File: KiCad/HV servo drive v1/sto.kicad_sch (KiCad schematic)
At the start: 41 parts, among them J9 Conn_02x03_Top_Bottom, Q8 PMOS, U16 6N137, U17 6N137, U18 FODM217A, U19 FODM217A

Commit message: KiCad 8.0 update
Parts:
- renumbered C97 to C96, C98 to C97, C96 to C98, D27 to D11, D26 to D25, D25 to D26, D28 to D27, D30 to D28, D29 to D7, J9 to J1, Q8 to Q7, R69 to R15, R73 to R16, R72 to R17, R77 to R31, R78 to R32, R83 to R65, R84 to R67, R79 to R69, R70 to R7, R71 to R70, R86 to R71, R85 to R72, R76 to R73, R80 to R74, R81 to R76, R74 to R77, R82 to R78, R67 to R8, R65 to R9, TP22 to TP18, TP23 to TP19, TP24 to TP20

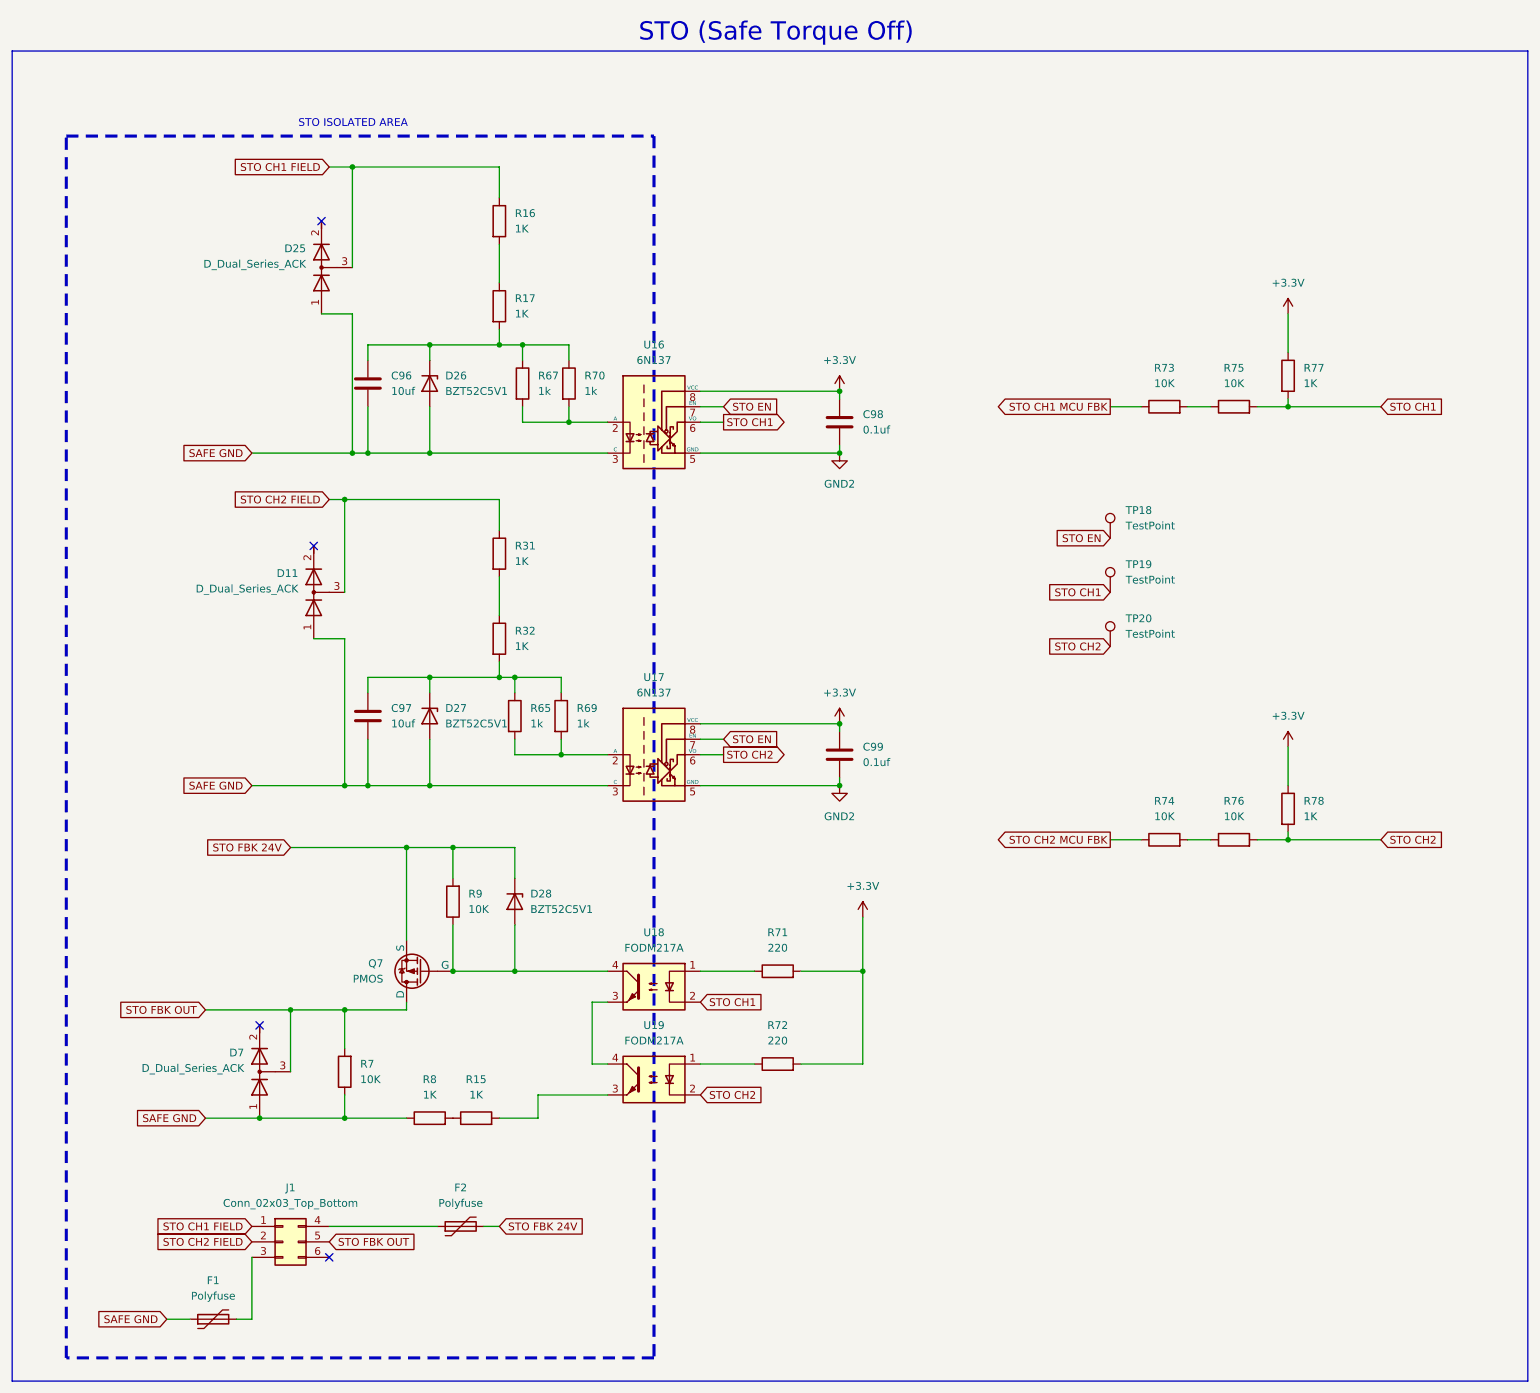
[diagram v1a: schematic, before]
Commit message: start rev 2 changes
fix component references, fix rj45 and dc-dc converter footprints, add RLC filters on all power connectors, add more mounting holes
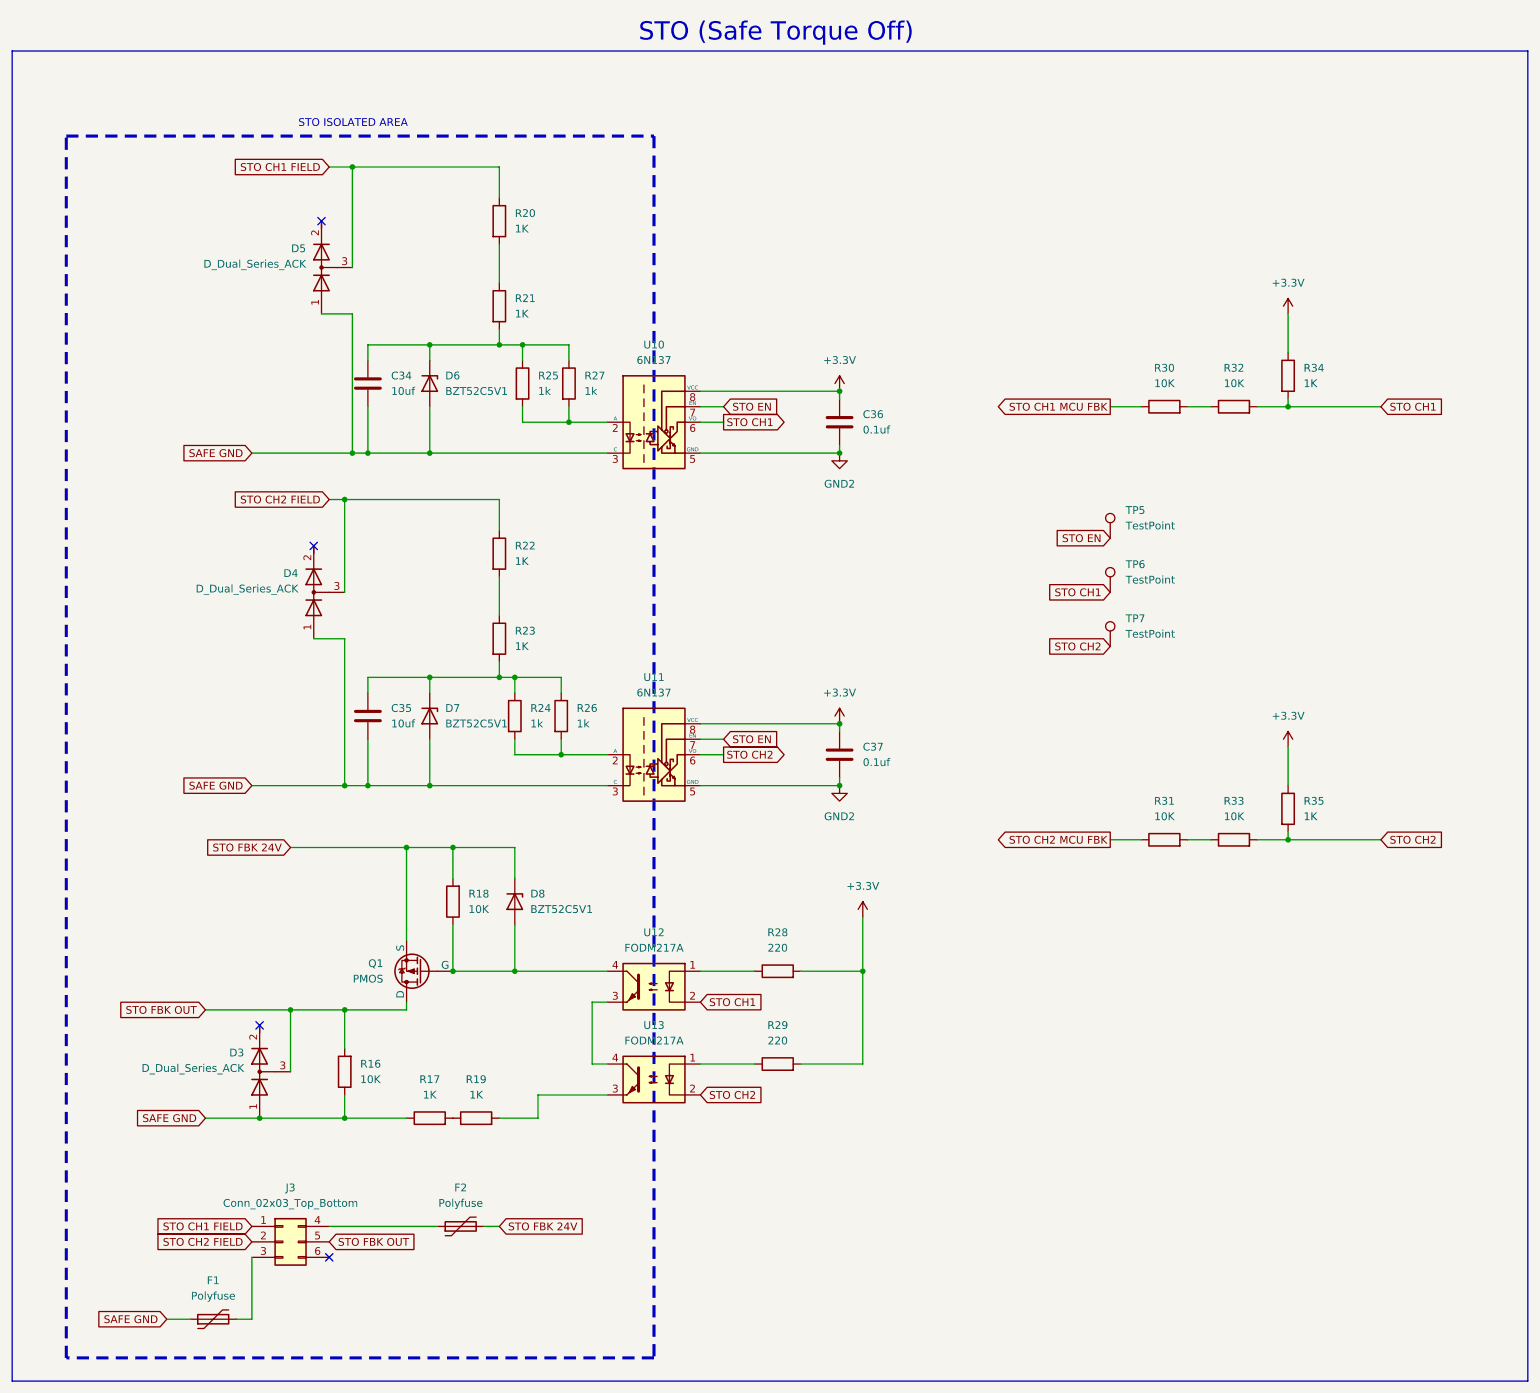
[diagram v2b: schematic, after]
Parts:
- renumbered C96 to C34, C97 to C35, C98 to C36, C99 to C37, D7 to D3, D11 to D4, D25 to D5, D26 to D6, D27 to D7, D28 to D8, J1 to J3, Q7 to Q1, R7 to R16, R8 to R17, R9 to R18, R15 to R19, R16 to R20, R17 to R21, R31 to R22, R32 to R23, R65 to R24, R67 to R25, R69 to R26, R70 to R27, R71 to R28, R72 to R29, R73 to R30, R74 to R31, R75 to R32, R76 to R33, R77 to R34, R78 to R35, TP18 to TP5, TP19 to TP6, TP20 to TP7, U16 to U10, U17 to U11, U18 to U12, U19 to U13

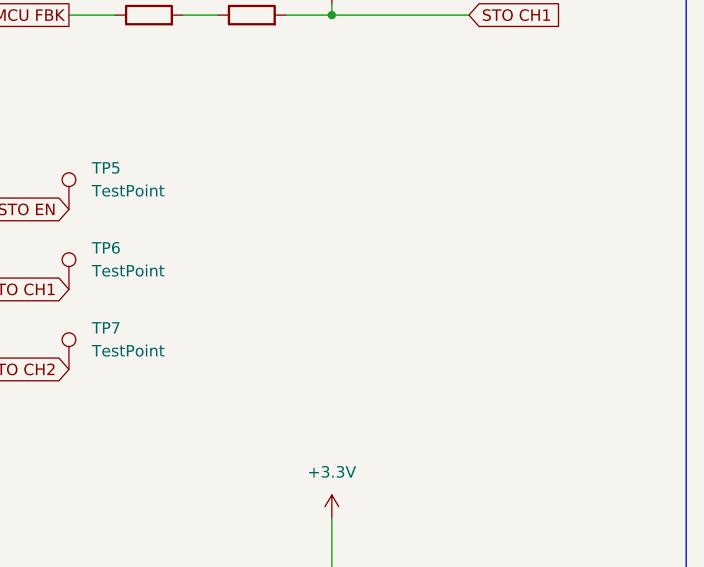
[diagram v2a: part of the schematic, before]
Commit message: add STO enable pulldown for MCU
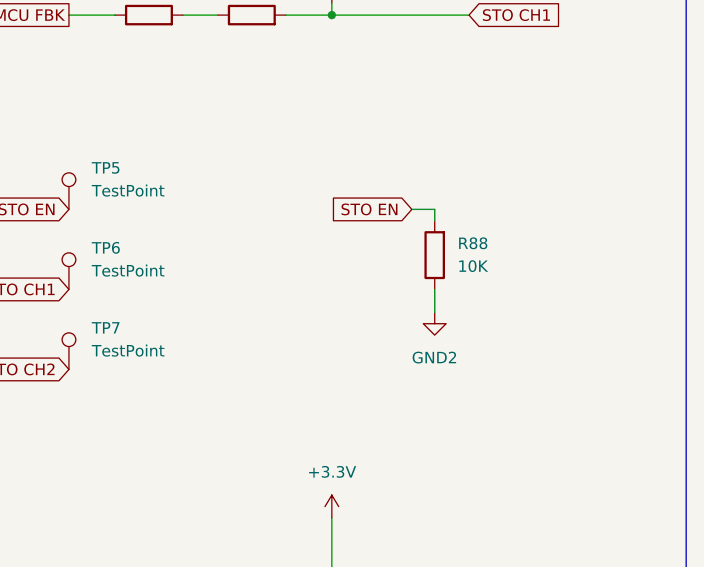
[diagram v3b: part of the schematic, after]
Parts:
- added R88: 10K, Resistor_SMD:R_0603_1608Metric, symbol Device:R
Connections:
- net GND2: now also R88.1
- net STO EN: now also R88.2
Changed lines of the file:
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@@
 	(wire
 		(pts
+			(xy 254 114.3) (xy 254 113.03)
+		)
+		(stroke
+			(width 0)
+			(type default)
+		)
+	)
+	(wire
+		(pts
 			(xy 226.06 91.44) (xy 229.87 91.44)
 		)
@@
 	(wire
 		(pts
+			(xy 251.46 113.03) (xy 254 113.03)
+		)
+		(stroke
+			(width 0)
+			(type default)
+		)
+	)
+	(wire
+		(pts
 			(xy 105.41 176.53) (xy 105.41 184.15)
 		)
@@
 	(wire
 		(pts
+			(xy 254 121.92) (xy 254 124.46)
+		)
+		(stroke
+			(width 0)
+			(type default)
+		)
+	)
+	(wire
+		(pts
 			(xy 124.46 81.28) (xy 116.84 81.28)
 		)
@@
 		)
 	)
+	(global_label "STO EN"
+		(shape input)
+		(at 251.46 113.03 180)
+		(fields_autoplaced yes)
+		(effects
+			(font
+				(size 1.27 1.27)
+			)
+			(justify right)
+		)
+		(property "Intersheetrefs" "${INTERSHEET_REFS}"
+			(at 241.5201 113.03 0)
+			(effects
+				(font
+					(size 1.27 1.27)
+				)
+				(justify right)
+				(hide yes)
+			)
+		)
+	)
 	(global_label "STO CH1"
 		(shape input)
@@
 	)
 	(symbol
+		(lib_id "Device:R")
+		(at 254 118.11 180)
+		(unit 1)
+		(exclude_from_sim no)
+		(in_bom yes)
+		(on_board yes)
+		(dnp no)
+		(fields_autoplaced yes)
+		(property "Reference" "R88"
+			(at 256.54 116.8399 0)
+			(effects
+				(font
+					(size 1.27 1.27)
+				)
+				(justify right)
+			)
+		)
+		(property "Value" "10K"
+			(at 256.54 119.3799 0)
+			(effects
+				(font
+					(size 1.27 1.27)
+				)
+				(justify right)
+			)
+		)
+		(property "Footprint" "Resistor_SMD:R_0603_1608Metric"
+			(at 255.778 118.11 90)
+			(effects
+				(font
+					(size 1.27 1.27)
+				)
+				(hide yes)
+			)
+		)
+		(property "Datasheet" "~"
+			(at 254 118.11 0)
+			(effects
+				(font
+					(size 1.27 1.27)
+				)
+				(hide yes)
+			)
+		)
+		(property "Description" ""
+			(at 254 118.11 0)
+			(effects
+				(font
+					(size 1.27 1.27)
+				)
+				(hide yes)
+			)
+		)
+		(pin "1"
+		)
+		(pin "2"
+		)
+		(instances
+			(project "HV servo drive v1"
+				(path "/00e1489f-e855-42b2-9b8a-dcc958a4feb6/5ac84363-ab69-4569-a1a9-ce084738114b"
+					(reference "R88")
+					(unit 1)
+				)
+			)
+		)
+	)
+	(symbol
 		(lib_id "Connector_Generic:Conn_02x03_Top_Bottom")
 		(at 77.47 228.6 0)
@@
 					(unit 1)
 				)
+			)
+		)
+	)
+	(symbol
+		(lib_id "power:GND2")
+		(at 254 124.46 0)
+		(unit 1)
+		(exclude_from_sim no)
+		(in_bom yes)
+		(on_board yes)
+		(dnp no)
+		(fields_autoplaced yes)
+		(property "Reference" "#PWR0141"
+			(at 254 130.81 0)
+			(effects
+				(font
+					(size 1.27 1.27)
+				)
+				(hide yes)
+			)
+		)
+		(property "Value" "GND2"
+			(at 254 129.54 0)
+			(effects
+				(font
+					(size 1.27 1.27)
+				)
+			)
+		)
+		(property "Footprint" ""
+			(at 254 124.46 0)
+			(effects
+				(font
+					(size 1.27 1.27)
+				)
+				(hide yes)
+			)
+		)
+		(property "Datasheet" ""
+			(at 254 124.46 0)
+			(effects
+				(font
+					(size 1.27 1.27)
+				)
+				(hide yes)
+			)
+		)
+		(property "Description" ""
+			(at 254 124.46 0)
+			(effects
+				(font
+					(size 1.27 1.27)
+				)
+				(hide yes)
+			)
+		)
+		(pin "1"
+		)
+		(instances
+			(project "HV servo drive v1"
+				(path "/00e1489f-e855-42b2-9b8a-dcc958a4feb6/5ac84363-ab69-4569-a1a9-ce084738114b"
+					(reference "#PWR0141")
+					(unit 1)
+				)
